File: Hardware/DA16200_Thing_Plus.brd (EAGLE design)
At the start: 22.9 x 59.7 mm, 103 parts, among them J2 THING_PLUS, J3 Qwiic, J5 USB C, J7 CORTEX_JTAG_DEBUG_PTH_NS, Q1 20V/4.2A/52mΩ/1.4W, U1 DA16200MOD, U2 CH340E_MSOP10, U3 MCP73831, U7 XC6222B331MR-G

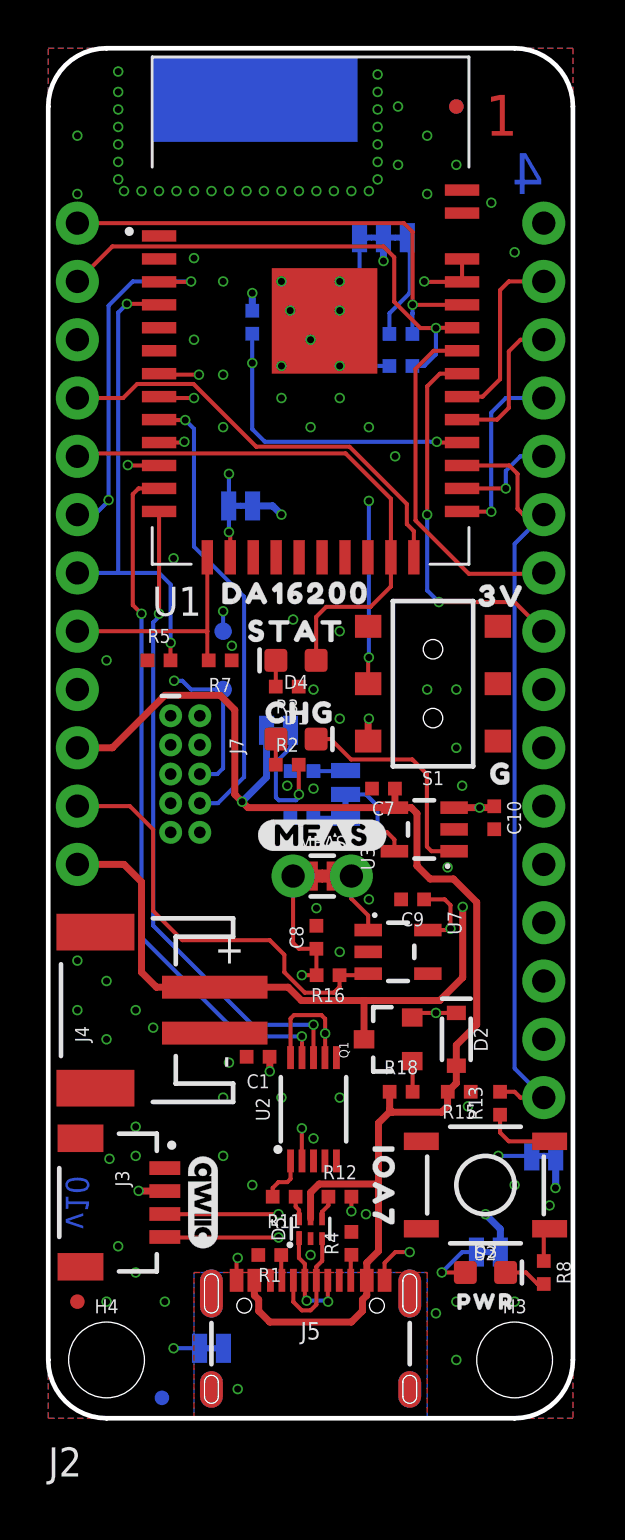
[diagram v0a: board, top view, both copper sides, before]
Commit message: Design review updates
Schematic:
* Remove "Ohm" from R11/R12 value
* Add schematic symbol for ground onto USB SHLD
Board:
* set layers in order
* Fix polygons to line up in DA16200 keep out area
* Add vias to stitch GND
* Fix some acid traps
* Evenly space out some traces
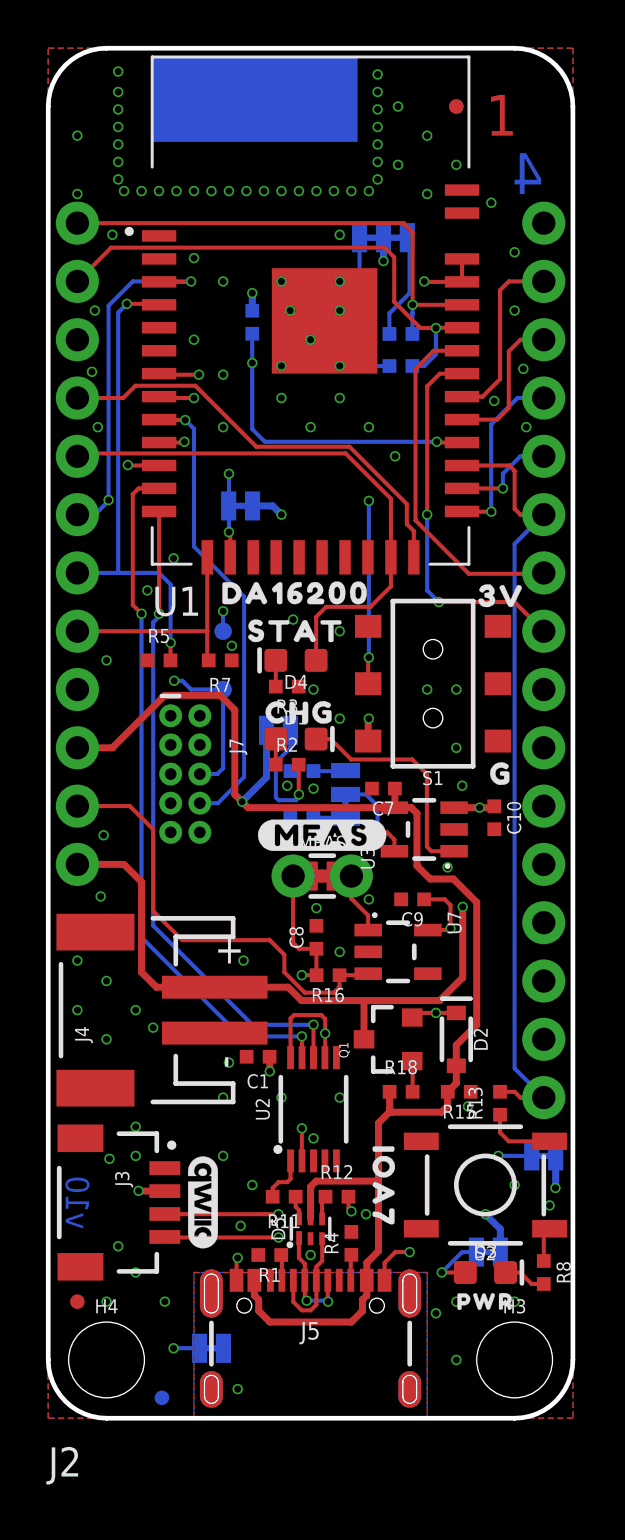
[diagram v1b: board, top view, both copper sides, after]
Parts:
- R11, R12: value 27OHM -> 27
- moved R12 0.13 mm to (12.6, 9.65)
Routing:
- net GND: vias 103 -> 117

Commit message: Design review updates
Change DRC to 4 layer minimum rules, lots of little updates to avoid overlap. Annular ring size increased
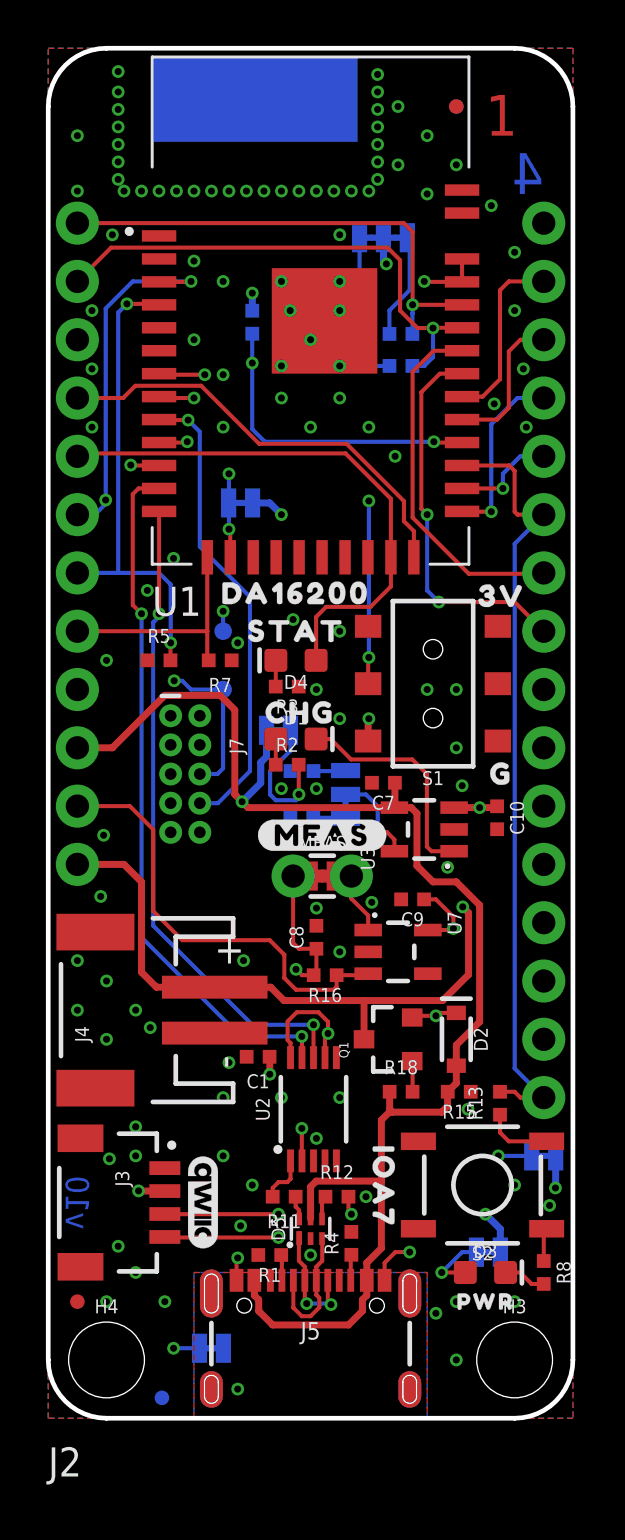
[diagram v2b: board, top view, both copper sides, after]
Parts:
- moved C7 0.25 mm to (14.6, 27.7)
- moved DA_MEAS 0.13 mm to (8.38, 39.9)
- moved S2 0.13 mm to (18.9, 10.2)
- moved R16 0.13 mm to (12.1, 19.3)
- moved C10 0.13 mm to (19.6, 26.2)
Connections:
- net SD_CS renamed GPIOA10
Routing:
- net N$15: track 15.6 -> 16.4 mm
- net N$6: track 5.19 -> 5.80 mm
- net V_USB: track 62.9 -> 63.5 mm

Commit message: Fixing buzzard labels
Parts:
- removed U$52: (no value), output:#VUB#0
- removed U$75: (no value), output:#SD#CS##0
- removed U$87: (no value), output:500MA0
- removed U$88: (no value), output:100MA0
- added U$14, U$15, U$18, U$19, U$20, U$40: (no value), output:#NC#0
- added U$21: (no value), output:5000
- added U$22: (no value), output:1000
- added U$23: (no value), output:MA0
- added U$24: (no value), output:SDA0
- added U$25: (no value), output:SCL0
- added U$26: (no value), output:#CSB#0
- added U$27: (no value), output:#IO10#0
- added U$28: (no value), output:110
- added U$32: (no value), output:100
- added U$33: (no value), output:RTC0
- added U$34: (no value), output:WK10
- added U$35: (no value), output:WK20
- added U$36: (no value), output:60
- added U$37: (no value), output:EN0
- added U$38: (no value), output:VUSB0
- added U$39: (no value), output:VBAT0
- added U$41: (no value), output:TX0
- added U$42: (no value), output:RX0
- added U$44: (no value), output:90
- added U$45: (no value), output:80
- added U$47: (no value), output:70
- added U$6: (no value), output:#VU#0
- moved U$13 4.70 mm to (14.6, 7.87), turned to 90 degrees
- moved U$3 1.02 mm to (17.9, 23.6)
- moved J7 0.13 mm to (6.10, 28.1)

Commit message: finish adding buzzard labels
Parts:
- added U$52: (no value), output:A20
- added U$54: (no value), output:A30
- added U$55: (no value), output:GND0
- added U$57: (no value), output:3V30
- added U$58: (no value), output:70
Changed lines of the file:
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@@
 <element name="U$45" library="output" package="80" value="" x="19.939" y="41.148" smashed="yes" rot="R90"/>
 <element name="U$47" library="output" package="70" value="" x="19.939" y="38.735" smashed="yes" rot="R90"/>
+<element name="U$52" library="output" package="A20" value="" x="18.669" y="37.846" smashed="yes"/>
+<element name="U$54" library="output" package="A30" value="" x="18.923" y="33.274" smashed="yes"/>
+<element name="U$55" library="output" package="GND0" value="" x="19.939" y="20.193" smashed="yes" rot="R90"/>
+<element name="U$57" library="output" package="3V30" value="" x="19.939" y="15.113" smashed="yes" rot="R90"/>
+<element name="U$58" library="output" package="70" value="" x="19.685" y="14.859" smashed="yes"/>
 </elements>
 <signals>

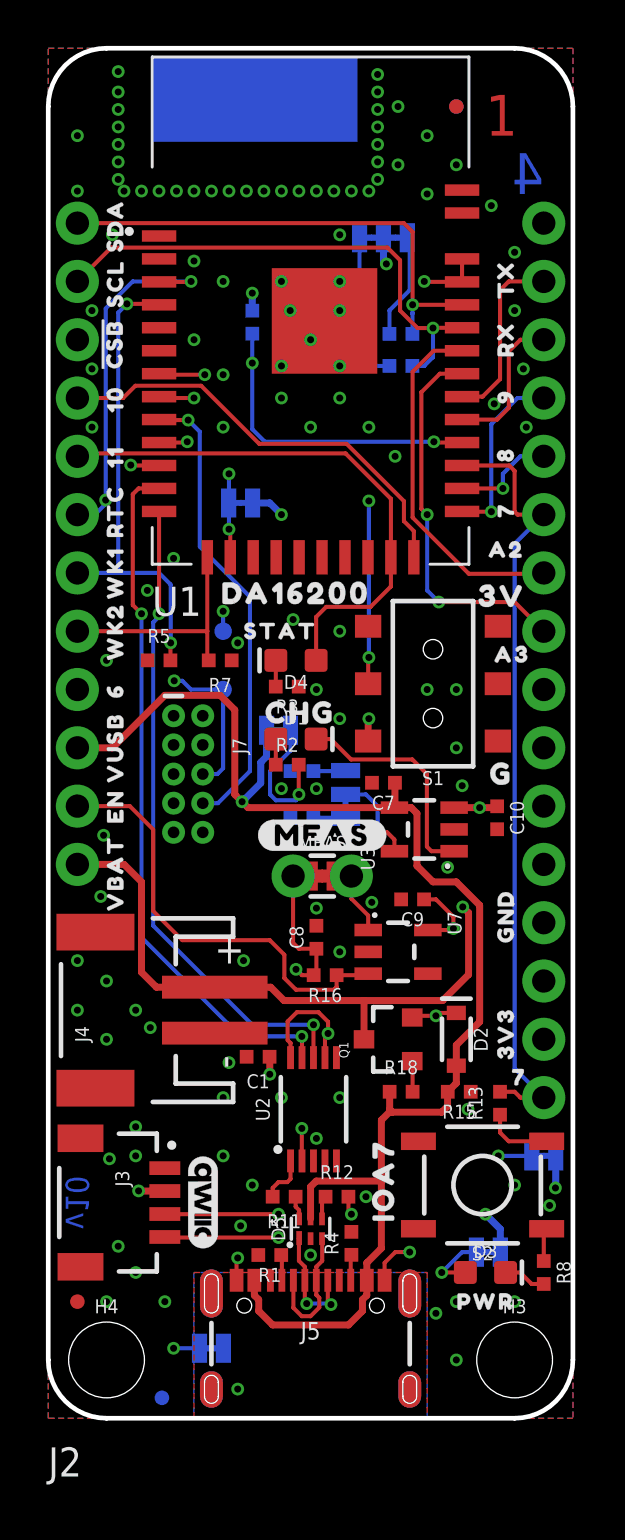
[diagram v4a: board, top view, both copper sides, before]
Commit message: Design review updates
* MEAS trace flipped to the bottom
* Move components from bottom of board to the top
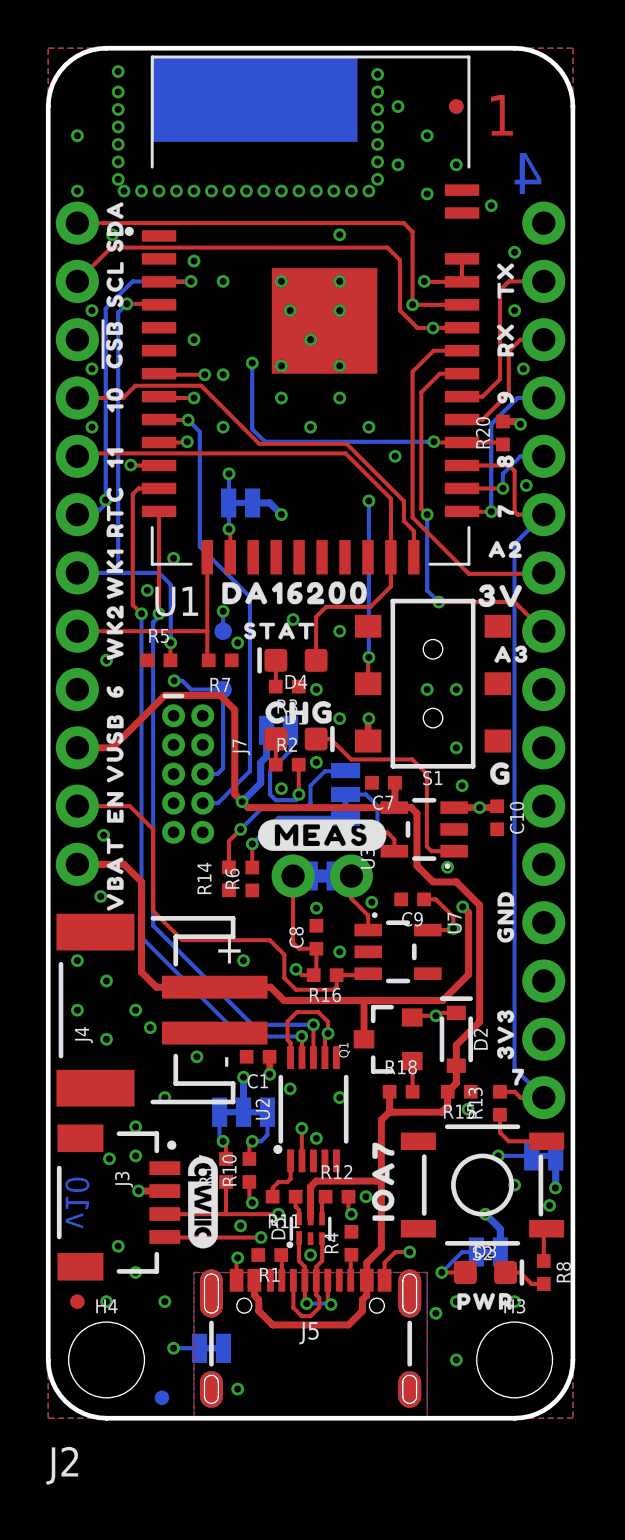
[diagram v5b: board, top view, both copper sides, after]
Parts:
- removed U$11: (no value), output:DA0
- removed U$12: (no value), output:#CH#0
- removed U$86: (no value), output:CHG0
- added U$59: (no value), output:#CHG#0
- added U$61: (no value), output:#DA_MEAS#0
- U$10: device output:MEAS0 -> output:#CH340#0
- moved I2C_PU 38.6 mm to (8.51, 13.3), turned to 180 degrees
- moved R17 37.2 mm to (7.75, 10.8), flipped to the top, turned to 90 degrees
- moved R10 35.7 mm to (8.76, 10.8), flipped to the top, turned to 90 degrees
- moved U$82 35.2 mm to (10.3, 15.1)
- moved U$10 31.6 mm to (20.7, 11.4)
- moved R20 11.9 mm to (19.8, 42.9), flipped to the top
- moved R14 5.67 mm to (7.87, 23.5), flipped to the top, turned to 90 degrees
- moved R6 3.43 mm to (8.89, 23.5), flipped to the top, turned to 90 degrees
- moved U$45 0.25 mm to (19.9, 40.9)
- flipped MEAS to the bottom, turned to 180 degrees
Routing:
- net N$20: track 1.41 -> 7.94 mm, vias 0 -> 1
- net N$10: track 1.42 -> 5.57 mm, vias 0 -> 1
- net N$2: track 6.58 -> 2.59 mm, vias 0 -> 1
- net N$3: track 4.60 -> 2.16 mm, vias 0 -> 1
- net SPI_CSB: track 21.6 -> 22.1 mm
- net I2C_SCL: track 72.7 -> 73.0 mm, vias 2 -> 3
- net GND: vias 117 -> 114
